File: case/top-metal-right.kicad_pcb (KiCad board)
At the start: 2 copper layers, 135 x 93.7 mm, 26 parts, among them SW1 SW_PUSH, SW10 SW_PUSH, SW11 SW_PUSH, SW12 SW_PUSH, SW13 SW_PUSH, SW14 SW_PUSH, SW15 SW_PUSH, SW16 SW_PUSH, SW17 SW_PUSH, SW18 SW_PUSH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

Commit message: update case files
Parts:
- moved RE1 6.76 mm to (195.1, 69.1)
- moved SW18 5.58 mm to (146.6, 117.6)
- moved SW19 5.58 mm to (167.8, 120.3)
- moved SW20 5.58 mm to (190.1, 124.1)
- moved H2 5.35 mm to (180.6, 118.1)
- moved H4 5.35 mm to (129.1, 104.1)
- moved H5 5.35 mm to (167.1, 72.1)
- moved SW10 5.35 mm to (175.6, 81.6)
- moved SW13 5.35 mm to (137.6, 94.1)
- moved SW14 5.35 mm to (156.6, 98.1)
- moved SW15 5.35 mm to (175.6, 100.6)
- moved SW3 5.35 mm to (137.6, 56.1)
- moved SW4 5.35 mm to (156.6, 60.1)
- moved SW5 5.35 mm to (175.6, 62.6)
- moved SW8 5.35 mm to (137.6, 75.1)
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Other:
- board size 135 x 93.7 mm -> 135 x 95.7 mm

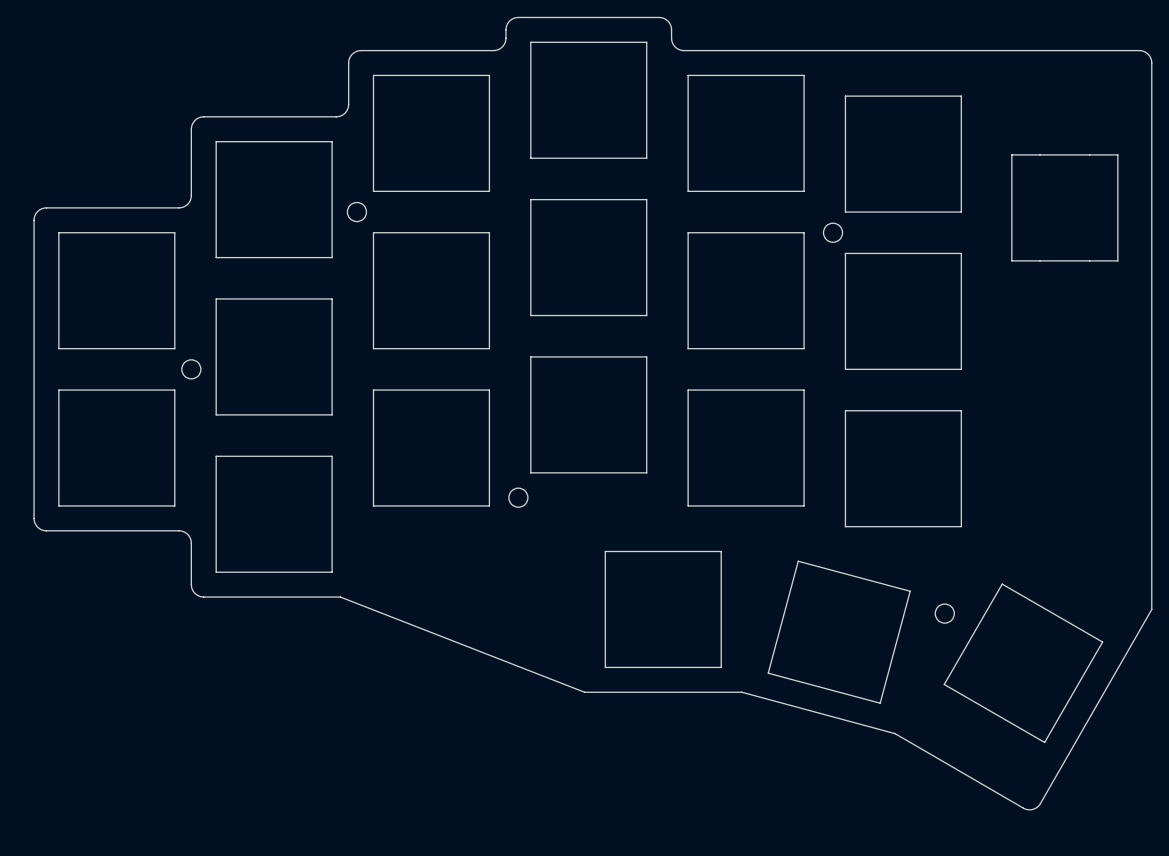
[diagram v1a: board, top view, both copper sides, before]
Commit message: separate plates
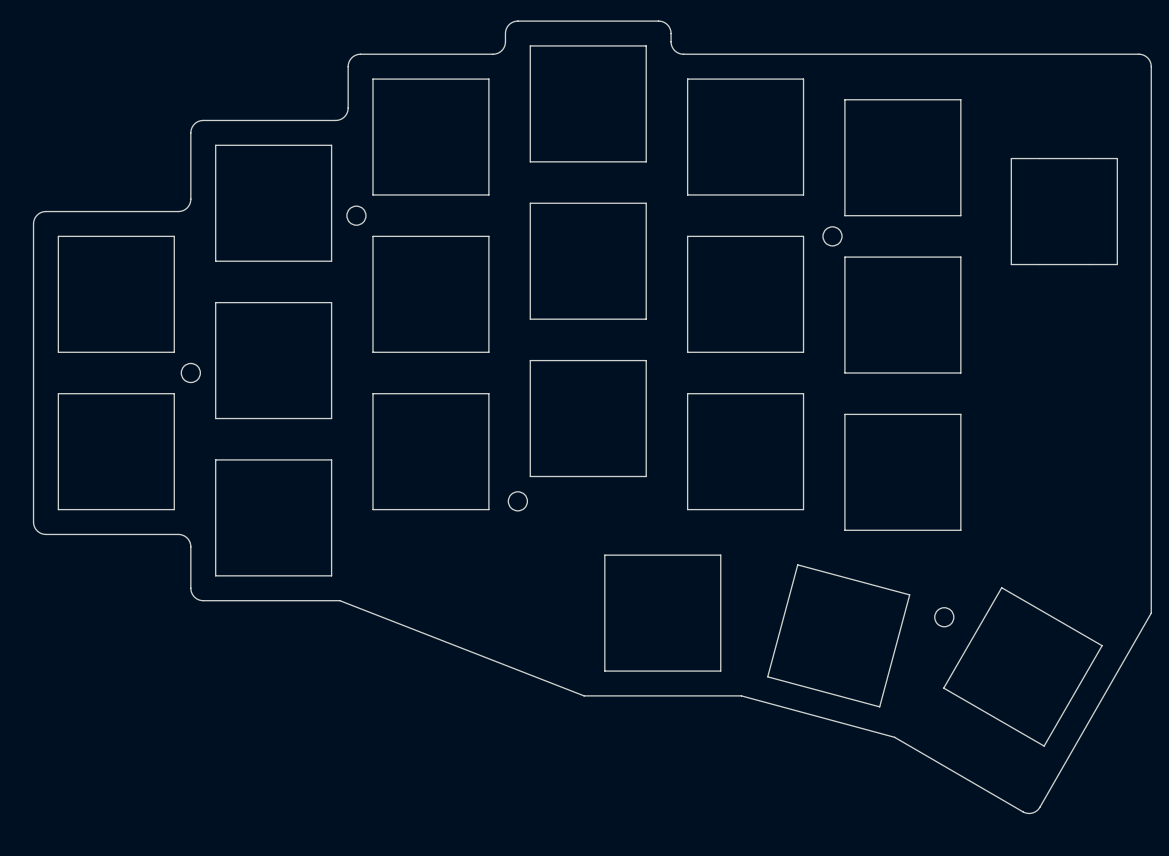
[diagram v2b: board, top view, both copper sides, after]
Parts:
- moved H2 0.44 mm to (180.5, 118.5)
- moved H4 0.44 mm to (129.0, 104.5)
- moved H5 0.44 mm to (167.0, 72.5)
- moved RE1 0.44 mm to (195.0, 69.5)
- moved SW10 0.44 mm to (175.5, 82.0)
- moved SW13 0.44 mm to (137.5, 94.5)
- moved SW14 0.44 mm to (156.5, 98.5)
- moved SW15 0.44 mm to (175.5, 101.0)
- moved SW18 0.44 mm to (146.5, 118.0)
- moved SW19 0.44 mm to (167.8, 120.8)
- moved SW20 0.44 mm to (190.0, 124.5)
- moved SW3 0.44 mm to (137.5, 56.5)
- moved SW4 0.44 mm to (156.5, 60.5)
- moved SW5 0.44 mm to (175.5, 63.0)
- moved SW8 0.44 mm to (137.5, 75.5)
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
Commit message: update cases, extra hole on right side
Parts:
- added H5: MountingHole, kbd:thread_m2, F.Cu at (199.0, 56.0)
- moved H1 0.71 mm to (109.0, 69.5)
- moved H2 0.71 mm to (180.0, 118.0)
- moved H3 0.71 mm to (89.0, 88.5)
- moved H4 0.71 mm to (128.5, 104.0)
- moved H5 0.71 mm to (166.5, 72.0)
- moved RE1 0.71 mm to (194.5, 69.0)
- moved SW1 0.71 mm to (99.0, 68.0)
- moved SW10 0.71 mm to (175.0, 81.5)
- moved SW11 0.71 mm to (99.0, 106.0)
- moved SW12 0.71 mm to (118.0, 98.0)
- moved SW13 0.71 mm to (137.0, 94.0)
- moved SW14 0.71 mm to (156.0, 98.0)
- moved SW15 0.71 mm to (175.0, 100.5)
- moved SW16 0.71 mm to (80.0, 79.0)
- moved SW17 0.71 mm to (80.0, 98.0)
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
